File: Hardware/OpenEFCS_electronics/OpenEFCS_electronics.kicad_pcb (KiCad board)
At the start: 2 copper layers, 88 x 17 mm, 68 parts, among them J1 15v, J2 GND, J3 M+, J4 M-, J5 CTRL-B, J6 PGRM, J7 CTRL-F, Q1 DMG3402L, Q2 BSC010N04LS6, Q3 BSC010N04LS6, SW1 DECOCK, U1 STM32F042K4Tx, U2 AP1117-33, U3 AOZ1282CI-1, U4 XJNG2103, U5 INA2180A4, Y1 8MHz 12pF

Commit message: Updated minor BOM mistake
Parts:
- D1: value MBR0530 -> GOODWORK K14
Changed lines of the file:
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@@
       (effects (font (size 0.6 0.6) (thickness 0.12)) (justify mirror))
     )
-    (fp_text value "MBR0530" (at 0 -2.1 90) (layer "B.Fab")
+    (fp_text value "GOODWORK K14" (at 0 -2.1 90) (layer "B.Fab")
       (effects (font (size 1 1) (thickness 0.15)) (justify mirror))
     )

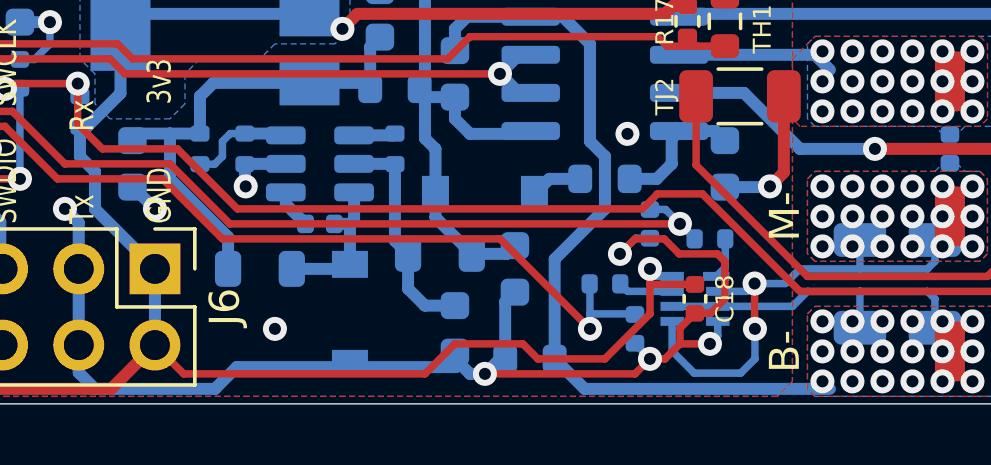
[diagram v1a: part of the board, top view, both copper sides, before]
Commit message: Release v0.3.1
Corrected footprint for INA2180
Regenerated manufacturing files
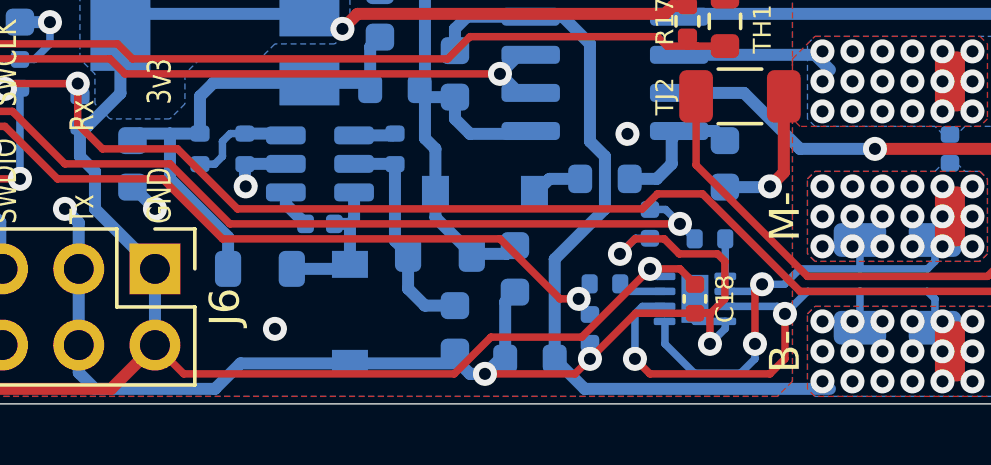
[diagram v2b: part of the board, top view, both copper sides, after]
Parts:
- U3: value AOZ1282CI-1 -> BL9342
- U5: footprint Package_DFN_QFN:OnSemi_DFN-8_2x2mm_P0.5mm -> Package_DFN_QFN:DFN-8-1EP_2x2mm_P0.5mm_EP0.9x1.6mm
- moved C19 1.50 mm to (88.0, 105.5)
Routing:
- net GNDPWR: track 38.0 -> 45.9 mm, vias 18 -> 20
- net /ISENSE_RUN_LP: track 43.3 -> 40.1 mm
- net GNDREF: track 107.7 -> 109.5 mm
- net +3V3: track 124.9 -> 123.0 mm

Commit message: design complete for second prototype
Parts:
- removed C5: 22u, Capacitor_SMD:C_0603_1608Metric
- removed J6: PGRM, Connector_PinHeader_2.54mm:PinHeader_2x05_P2.54mm_Vertical
- removed J7: CTRL-F, Connector_JST:JST_GH_BM08B-GHS-TBT_1x08-1MP_P1.25mm_Vertical
- removed Ris1, Ris2: 0.5m, Resistor_SMD:R_1206_3216Metric
- removed TJ2: Thermal Jumper, Resistor_SMD:R_1206_3216Metric
- removed TVS1: SMDJ15A-HR, Diode_SMD:D_SMC
- removed Y1: 8MHz 12pF, Crystal:Crystal_SMD_3225-4Pin_3.2x2.5mm
- added C20: 100n, Capacitor_SMD:C_0603_1608Metric, F.Cu at (168.5, -15.5)
- added CIN1: 22uF, Capacitor_Tantalum_SMD:CP_EIA-3528-12_Kemet-T, B.Cu at (135.8, -22.8)
- added D5: GOODWORK K14, Diode_SMD:D_SOD-123, F.Cu at (151.2, -10.0)
- added F1: 3557, KiCAD-Custom-Lib:Keystone 3557, F.Cu at (147.0, -22.5)
- added JP1: BYP, Jumper:SolderJumper-2_P1.3mm_Open_TrianglePad1.0x1.5mm, B.Cu at (161.0, -25.0)
- added R21: 56k, Resistor_SMD:R_0603_1608Metric, F.Cu at (167.5, -10.0)
- added R22: 10k, Resistor_SMD:R_0603_1608Metric, B.Cu at (164.5, -10.5)
- added SW2: CONF, Button_Switch_SMD:SW_SPST_B3U-1000P, F.Cu at (182.0, -23.0)
- added TP1: NTC, TestPoint:TestPoint_Pad_1.0x1.0mm, F.Cu at (166.5, -13.0)
- added TP10: BVS, TestPoint:TestPoint_Pad_1.0x1.0mm, F.Cu at (165.0, -13.0)
- added TP11: ISF, TestPoint:TestPoint_Pad_1.0x1.0mm, F.Cu at (168.0, -13.0)
- added TP2: PML, TestPoint:TestPoint_Pad_1.0x1.0mm, F.Cu at (169.5, -11.5)
- added TP3: PMH, TestPoint:TestPoint_Pad_1.0x1.0mm, F.Cu at (169.5, -13.0)
- added TP4: TRC, TestPoint:TestPoint_Pad_1.0x1.0mm, F.Cu at (166.5, -25.2)
- added TP5: ISR, TestPoint:TestPoint_Pad_1.0x1.0mm, F.Cu at (166.5, -17.0)
- added TP6: SIO, TestPoint:TestPoint_Pad_1.0x1.0mm, F.Cu at (166.5, -22.0)
- added TP7: B0, TestPoint:TestPoint_Pad_1.0x1.0mm, F.Cu at (168.0, -22.0)
- added TP8: RST, TestPoint:TestPoint_Pad_1.0x1.0mm, F.Cu at (168.0, -20.5)
- added TP9: SCK, TestPoint:TestPoint_Pad_1.0x1.0mm, F.Cu at (165.0, -25.2)
- C1, C19, C6, C8: footprint Capacitor_SMD:C_0402_1005Metric -> Capacitor_SMD:C_0603_1608Metric; moved to F.Cu
- C10, C13, C16, C17: value 100n -> 10u; footprint Capacitor_SMD:C_0402_1005Metric -> Capacitor_SMD:C_0805_2012Metric
- C11, C7: footprint Capacitor_SMD:C_0402_1005Metric -> Capacitor_SMD:C_0603_1608Metric
- C12: value 4.7u -> 100n; footprint Capacitor_SMD:C_0402_1005Metric -> Capacitor_SMD:C_0603_1608Metric; moved to F.Cu
- C14, C3: value 10u -> 100n
- C15: footprint Capacitor_SMD:C_0603_1608Metric -> Capacitor_SMD:C_0805_2012Metric; moved to F.Cu
- C18: footprint Capacitor_SMD:C_0402_1005Metric -> Capacitor_SMD:C_0603_1608Metric; moved to B.Cu
- C2, C4: footprint Capacitor_SMD:C_0603_1608Metric -> Capacitor_SMD:C_0805_2012Metric
- C9: value 22u -> 100n
- D1, D2, D3, Q1, Q2, Q3, R1, R15, U3: moved to F.Cu
- D4: value GOODWORK K14 -> YLW; footprint Diode_SMD:D_SOD-123 -> LED_SMD:LED_0603_1608Metric; moved to F.Cu
- J1, J2, J3, J4, TH1: moved to B.Cu
- J5: value CTRL-B -> CTRL; footprint Connector_PinHeader_2.00mm:PinHeader_1x08_P2.00mm_Vertical -> Connector_JST:JST_PH_B8B-PH-K_1x08_P2.00mm_Vertical; moved to F.Cu
- L1, L2: value 10uH -> 6.8uH
- R10: value 1.5k -> 56k; footprint Resistor_SMD:R_0402_1005Metric -> Resistor_SMD:R_0603_1608Metric; moved to F.Cu
- R11, R12, R16, R5: footprint Resistor_SMD:R_0402_1005Metric -> Resistor_SMD:R_0603_1608Metric; moved to F.Cu
- R13: value 1R8 -> 1.5k
- R17: value 1.5k -> 10k; footprint Resistor_SMD:R_0402_1005Metric -> Resistor_SMD:R_0603_1608Metric; moved to B.Cu
- R18: value 1.5k -> 1R8; footprint Resistor_SMD:R_0402_1005Metric -> Resistor_SMD:R_0603_1608Metric; moved to F.Cu
- R19: value 56k -> 1.5k; footprint Resistor_SMD:R_0402_1005Metric -> Resistor_SMD:R_0603_1608Metric
- R2: value 10k -> 56k; footprint Resistor_SMD:R_0402_1005Metric -> Resistor_SMD:R_0603_1608Metric; moved to F.Cu
- R20: value 10k -> 1.5k; footprint Resistor_SMD:R_0402_1005Metric -> Resistor_SMD:R_0603_1608Metric; moved to F.Cu
- R3, R6, R7: footprint Resistor_SMD:R_0402_1005Metric -> Resistor_SMD:R_0603_1608Metric
- R4: value 1R8 -> 10k
- R8: value 0 -> 56k; moved to F.Cu
- R9: value 56k -> 10k; footprint Resistor_SMD:R_0402_1005Metric -> Resistor_SMD:R_0603_1608Metric
- SW1: value DECOCK -> PREC; footprint Button_Switch_SMD:SW_SPST_B3U-3000P -> Button_Switch_SMD:SW_SPST_B3U-1000P
- TJ1: value Thermal Jumper -> ThermJmpr; moved to B.Cu
- U2: value AP1117-33 -> AP2204K-3.3; footprint Package_TO_SOT_SMD:SOT-223-3_TabPin2 -> Package_TO_SOT_SMD:SOT-23-5; moved to F.Cu
- U5: value INA2180A4 -> INA194; footprint Package_DFN_QFN:DFN-8-1EP_2x2mm_P0.5mm_EP0.9x1.6mm -> Package_TO_SOT_SMD:SOT-23-5
- moved J5 184.6 mm to (177.6, -24.0), turned to -90 degrees
- moved R9 180.7 mm to (180.5, -23.0), turned to -90 degrees
- moved Q1 178.6 mm to (172.5, -24.5), turned to 0 degrees
- moved R2 169.0 mm to (172.5, -20.0), turned to 0 degrees
- moved C11 167.6 mm to (182.0, -23.0), turned to -90 degrees
- moved C1 167.2 mm to (169.0, -19.0), turned to 0 degrees
- moved R11 163.5 mm to (164.0, -15.5)
- moved C8 162.2 mm to (159.5, -23.0), turned to 0 degrees
- moved U1 161.3 mm to (168.0, -19.5), turned to 180 degrees
- moved C9 159.5 mm to (172.5, -24.5), turned to 90 degrees
- moved C3 157.4 mm to (179.8, -19.0), turned to 90 degrees
- moved C12 157.0 mm to (172.5, -18.5), turned to 180 degrees
- moved R10 156.6 mm to (168.5, -24.0)
- moved R12 156.4 mm to (168.5, -25.5)
- moved C6 154.8 mm to (159.2, -10.0), turned to 180 degrees
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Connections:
- C10 pad 1: /DECOCK -> +5V
- C11 pad 1: +3V3 -> /CONF
- C13 pad 1: /M+ -> +3V3
- C13 pad 2: /ISENSE_RAW -> GNDREF
- C14 pad 1: +15V -> /M+
- C15 pad 1: /M+ -> +15V
- C15 pad 2: Net-(C15-Pad2) -> GNDPWR
- C16 pad 1: /ISENSE_BRAKE_LP -> +15V
- C16 pad 2: GNDREF -> GNDPWR
- C17 pad 1: /BATT_SENSE -> /M+
- C17 pad 2: GNDREF -> Net-(C17-Pad2)
- C18 pad 1: +3V3 -> GNDREF
- C18 pad 2: GNDREF -> +3V3
- C19 pad 1: /ISENSE_RUN_LP -> /BATT_SENSE
- C3 pad 1: Net-(C3-Pad1) -> /AIN1
- C4 pad 1: +5V -> Net-(C4-Pad1)
- C7 pad 1: Net-(C7-Pad1) -> /PREC
- C7 pad 2: Net-(C7-Pad2) -> GNDREF
- C8 pad 1: +3V3 -> Net-(C8-Pad1)
- C8 pad 2: GNDREF -> Net-(C8-Pad2)
- C9 pad 1: +5V -> +3V3
- D1 pad 1: Net-(C7-Pad2) -> Net-(C8-Pad2)
- D4 pad 1: Net-(D4-Pad1) -> +15V
- D4 pad 2: +15V -> Net-(D4-Pad2)
- J1 pad 1: +15V -> +BATT
- J4 pad 1: /ISENSE_RAW -> GNDPWR
- L1 pad 2: Net-(C3-Pad1) -> Net-(C4-Pad1)
- L2 pad 1: Net-(C7-Pad2) -> Net-(C8-Pad2)
- R10 pad 1: Net-(D2-Pad2) -> GNDREF
- R10 pad 2: +3V3 -> /Tracer
- R11 pad 1: Net-(Q1-Pad1) -> Net-(D2-Pad2)
- R11 pad 2: /Tracer -> +3V3
- R12 pad 1: Net-(D3-Pad2) -> Net-(Q1-Pad1)
- R12 pad 2: +3V3 -> /Tracer
- R13 pad 1: Net-(Q2-Pad4) -> Net-(D3-Pad2)
- R13 pad 2: /HB_HIGH -> +3V3
- R14 pad 1: Net-(Q3-Pad4) -> Net-(Q2-Pad4)
- R14 pad 2: /HB_LOW -> /HB_HIGH
- R15 pad 1: Net-(C15-Pad2) -> Net-(Q3-Pad4)
- R15 pad 2: Net-(D4-Pad1) -> /HB_LOW
- R16 pad 1: /ISENSE_BRAKE_LP -> +BATT
- R16 pad 2: /ISENSE_BRAKE -> Net-(D4-Pad2)
- R17 pad 1: /NTC -> GNDREF
- R17 pad 2: +3V3 -> +15V
- R18 pad 1: /ISENSE_RUN_LP -> Net-(C17-Pad2)
- R18 pad 2: /ISENSE_RUN -> Net-(D5-Pad1)
- R19 pad 1: /BATT_SENSE -> /NTC
- R19 pad 2: +15V -> +3V3
- R20 pad 1: GNDREF -> /ISENSE_RUN_LP
- R20 pad 2: /BATT_SENSE -> /ISENSE_RUN
- R3 pad 1: Net-(R3-Pad1) -> /AIN1
- R3 pad 2: Net-(C3-Pad1) -> +3V3
- R4 pad 1: Net-(C5-Pad1) -> Net-(R4-Pad1)
- R4 pad 2: +3V3 -> Net-(C4-Pad1)
- R7 pad 1: /DECOCK -> /PREC
- R8 pad 1: +5V -> GNDREF
- R8 pad 2: +15V -> /BOOT0
- R9 pad 1: GNDREF -> /CONF
- R9 pad 2: /Tracer -> +3V3
- SW1 pad 2: /DECOCK -> /PREC
- U1 pad 10: /ISENSE_RUN_LP -> /PREC
- U1 pad 11: /ISENSE_BRAKE_LP -> /PWMH
- U1 pad 12: /PWMMOT -> /PWML
- U1 pad 13: /NTC -> /ISENSE_RUN_LP
- U1 pad 14: unconnected-(U1-Pad14) -> /NTC
- U1 pad 19: /Tx -> /LED1
- U1 pad 2: /OSCIN -> /CONF
- U1 pad 20: /Rx -> unconnected-(U1-Pad20)
- U1 pad 21: /LED1 -> unconnected-(U1-Pad21)
- U1 pad 22: /DECOCK -> unconnected-(U1-Pad22)
- U1 pad 3: /OSCOUT -> unconnected-(U1-Pad3)
- U2 pad 1: GNDREF -> +5V
- U2 pad 2: +3V3 -> GNDREF
- U3 pad 1: Net-(C7-Pad1) -> Net-(C8-Pad1)
- U3 pad 4: Net-(R3-Pad1) -> Net-(R4-Pad1)
- U3 pad 5: Net-(C3-Pad1) -> Net-(C4-Pad1)
- U3 pad 6: Net-(C7-Pad2) -> Net-(C8-Pad2)
- U4 pad 2: /PWMMOT -> /PWMH
- U4 pad 3: /PWMMOT -> /PWML
- U4 pad 8: Net-(C15-Pad2) -> Net-(C17-Pad2)
- U5 pad 1: /ISENSE_BRAKE -> /ISENSE_RUN
- U5 pad 2: /ISENSE_RAW -> GNDREF
- U5 pad 3: GNDPWR -> +15V
- U5 pad 4: GNDREF -> /M+
- U5 pad 5: /ISENSE_RAW -> +3V3
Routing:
- net +3V3: track 123.0 -> 50.7 mm, vias 7 -> 5
- net GNDREF: track 109.5 -> 41.8 mm, vias 24 -> 26
- net /DECOCK: track 64.0 -> 0.00 mm, vias 4 -> 0
- net /ISENSE_BRAKE_LP: track 42.0 -> 0.00 mm, vias 2 -> 0
- net /PWMMOT: track 33.3 -> 0.00 mm, vias 2 -> 0
- net /ISENSE_RUN_LP: track 40.1 -> 8.53 mm
- net +15V: track 72.8 -> 42.9 mm, vias 22 -> 13
- net /NTC: track 37.6 -> 12.5 mm, vias 1 -> 2
- net /PWML: track 0.00 -> 23.3 mm, vias 0 -> 2
- net /PREC: track 0.00 -> 22.6 mm, vias 0 -> 2
- net /PWMH: track 0.00 -> 22.6 mm, vias 0 -> 2
- net GNDPWR: track 45.9 -> 23.5 mm, vias 20 -> 15
- net /ISENSE_RUN: track 1.58 -> 22.4 mm, vias 0 -> 2
- net /CONF: track 0.00 -> 17.3 mm, vias 0 -> 1
- net /ISENSE_RAW: track 16.0 -> 0.00 mm, vias 20 -> 0
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- added copper zone on In1.Cu, net +15V
- added copper zone on In2.Cu, net +15V
- added copper zone on In1.Cu, net +3V3
- added copper zone on B.Cu, net +BATT
- added copper zone on In1.Cu, net /M+
- added copper zone on In2.Cu, net /M+
- added copper zone on In2.Cu, net GNDREF
- removed copper zone on B.Cu, net +3V3
- removed copper zone on B.Cu, net /ISENSE_RAW
- removed copper zone on F.Cu, net /ISENSE_RAW
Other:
- board size 88 x 17 mm -> 50 x 19 mm
- copper layers 2 -> 4
- board text added: "15v"
- board text added: "3v3 GND"
- board text added: "B0"
- board text added: "BVS"
- board text added: "CONF"
- board text added: "ISF"
- board text added: "ISR"
- board text added: "NTC"
- board text added: "PGND"
- board text added: "PMH"
- board text added: "PML"
- board text added: "PREC"
- board text added: "RST"
- board text added: "SCK"
- board text added: "SIO"
- board text added: "TCR-"
- board text added: "TRC"
- board text added: "TRG AIN Tx Rx"
- board text removed: "B-"
- board text removed: "M-"
- board text removed: "RST BOOT0 NC NC SWDIO SWCLK Tx Rx GND 3v3"
